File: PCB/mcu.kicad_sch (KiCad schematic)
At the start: 15 parts

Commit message: ok stm32
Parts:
- removed C? (x5): 100n, symbol Device:C
- removed C?: 10n, symbol Device:C
- removed C? (x3): 1u, symbol Device:C
- removed C?: 2.7u, symbol Device:C
- removed C?: 10u, symbol Device:C
- removed FB?: FerriteBead, symbol Device:FerriteBead
- removed R?: 1, symbol Device:R
- removed U?: EFM32PG22C200F128IM32-C, Package_DFN_QFN:QFN-32-1EP_4x4mm_P0.4mm_EP2.9x2.9mm, symbol TattooSupplyLib:EFM32PG22C200F128IM32-C
- added C? (x5): 100n, symbol Device:C
- added C? (x2): 20p, symbol Device:C
- added C?: 1u, symbol Device:C
- added C?: 10n, symbol Device:C
- added C?: 4.7u, symbol Device:C
- added FB?: FerriteBead, symbol Device:FerriteBead
- added J?: Conn_ARM_SWD_TagConnect_TC2030-NL, Connector:Tag-Connect_TC2030-IDC-NL_2x03_P1.27mm_Vertical, symbol Connector:Conn_ARM_SWD_TagConnect_TC2030-NL
- added JP?: Jumper_3_Open, symbol Jumper:Jumper_3_Open
- added NT?: NetTie_2, symbol Device:NetTie_2
- added R?: 10k, symbol Device:R
- added R? (x3): 100k, symbol Device:R
- added R?: R, symbol Device:R
- added R?: DNP, symbol Device:R
- added R? (x2): 4.7k, symbol Device:R
- added SW?: SW_Push, symbol Switch:SW_Push
- added U?: STM32F103C8Tx, Package_QFP:LQFP-48_7x7mm_P0.5mm, symbol MCU_ST_STM32F1:STM32F103C8Tx
- added Y?: Crystal, symbol Device:Crystal
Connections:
- net GND: now also J?.3 (GND), J?.5 (GND), J?.9 (GNDDetect), C?.2, C?.2, C?.2, C?.2, C?.2, C?.2, C?.2, C?.2, C?.2, C?.2, J?.5 (GND), JP?.3 (B), NT?.1, R?.1, R?.2, SW?.2, U?.23 (VSS), U?.35 (VSS), U?.47 (VSS)
- net V_{IN}: now reaches J?.1 (VTref)
- net V_{IN}: now also C?.1, C?.1, C?.1, C?.1, C?.1, FB?.1, J?.1 (VCC), JP?.1 (A), R?.1, R?.1, R?.1, R?.1, U?.1 (VBAT), U?.24 (VDD), U?.36 (VDD), U?.48 (VDD)
- net ~{RESET}: now reaches J?.10 (~{RESET})
- net ~{RESET}: now also C?.1, J?.3 (~{RESET}), R?.2, SW?.1, U?.7 (NRST)
- net SWDIO: now reaches J?.2 (SWDIO/TMS)
- net SWDIO: now also J?.2 (SWDIO), U?.34 (PA13)
- net SWCLK: now reaches J?.4 (SWDCLK/TCK)
- net SWCLK: now also J?.4 (SWCLK), U?.37 (PA14)
- new net: C?.1, R?.1, Y?.2
- new net: R?.2, U?.20 (PB2)
- new net: JP?.2 (C), R?.2
- new net: R?.1, R?.2, U?.44 (BOOT0)
- new net: NT?.2, U?.8 (VSSA)
- new net Analog1: U?.10 (PA0)
- new net Analog2: U?.11 (PA1)
- new net Display.MISO: U?.16 (PA6)
- new net Display.MOSI: U?.17 (PA7)
- new net Display.SCK: U?.15 (PA5)
- new net Display.~{CS}: U?.14 (PA4)
- new net I2C.SCL: R?.2, U?.42 (PB6)
- new net I2C.SDA: R?.2, U?.43 (PB7)
- new net OSC_{IN}: C?.1, U?.5 (PD0), Y?.1
- new net OSC_{OUT}: R?.2, U?.6 (PD1)
- new net SW1: U?.29 (PA8)
- new net SW2: U?.30 (PA9)
- new net USB.D+: U?.33 (PA12)
- new net USB.D-: U?.32 (PA11)
- new net USB_DFU: R?.1, U?.38 (PA15)
- new net VDDA: C?.1, C?.1, FB?.2, U?.9 (VDDA)
- no-connect marks 1 -> 22
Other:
- note added: "AN2867 : ECS-80-18-5PX-TR NX5032GA-8.000M-STD-CSU-1 BEST"
- note removed: "AVDD"
- note removed: "DVDD"
- note removed: "EFM32PG22C200F128IM32-C"
- note removed: "IOVDD"
- note removed: "VREG_{VDD}"
- moved on the sheet: J?

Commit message: continue quartz
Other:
- note added: "AN2867 : ABM3B-8.000MHZ-B2-T C_{L}=18pF C_{S}=10pF C_{L}-C_{S}=(C_{L1}*"
- note removed: "AN2867 : ECS-80-18-5PX-TR NX5032GA-8.000M-STD-CSU-1 BEST"
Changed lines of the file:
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@@
     (stroke (width 0) (type default) (color 0 0 0 0))
   )
-  (text "AN2867 :\nECS-80-18-5PX-TR\nNX5032GA-8.000M-STD-CSU-1 BEST\n"
+  (text "AN2867 :\nABM3B-8.000MHZ-B2-T\nC_{L}=18pF\nC_{S}=10pF\nC_{L}-C_{S}=(C_{L1}*\n"
     (at 21.59 101.6 0)
     (effects (font (size 1.27 1.27)) (justify left bottom))

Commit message: ok mcu
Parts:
- removed J?: Conn_ARM_JTAG_SWD_10, symbol Connector:Conn_ARM_JTAG_SWD_10
- removed R?: 10k, symbol Device:R
- added C? (x3): 100n, symbol Device:C
- added J?: Conn_ST_STDC14, symbol Connector:Conn_ST_STDC14
- added J?: Conn_01x03, symbol Connector_Generic:Conn_01x03
- added R? (x3): 10k, symbol Device:R
- added R? (x2): 20, symbol Device:R
- added SW?: RotaryEncoder_Switch, symbol Device:RotaryEncoder_Switch
- R?: value R -> 953
- Y?: value Crystal -> ABM3B-8.000MHZ-B2-T; footprint (none) -> Crystal:Crystal_SMD_Abracon_ABM3B-4Pin_5.0x3.2mm
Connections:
- net GND: now also C?.1, C?.2, C?.2, J?.11 (GNDDetect), J?.3 (Pin_3), J?.5 (GND), J?.7 (GND), SW?.C, SW?.S2
- net SW1: now also R?.2; no longer U?.29 (PA8)
- net SW2: now also R?.2; no longer U?.30 (PA9)
- net SWCLK: now also J?.6 (JCLK/SWCLK)
- net SWDIO: now also J?.4 (JTMS/SWDIO)
- net V_{IN}: now also J?.3 (VCC), R?.1, R?.2, R?.2
- net ~{RESET}: now also J?.12 (~{RST})
- net Debug.Tx: now reaches U?.12 (PA2)
- net Debug.Tx: now also J?.1 (Pin_1), J?.14 (VCP_TX)
- net Debug.Rx: now reaches U?.13 (PA3)
- net Debug.Rx: now also J?.13 (VCP_RX), J?.2 (Pin_2)
- net Encod.DT: now reaches U?.26 (PB13)
- net Encod.DT: now also C?.2, R?.1, SW?.A
- net Encod.CLK: now reaches U?.27 (PB14)
- net Encod.CLK: now also C?.1, R?.2, SW?.B
- net Encod.SW: now reaches U?.28 (PB15)
- net Encod.SW: now also C?.1, R?.1, SW?.S1
- new net: R?.1, U?.29 (PA8)
- new net: R?.1, U?.30 (PA9)
- no-connect marks 22 -> 18
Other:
- note added: "AN2867 : ABM3B-8.000MHZ-B2-T C_{L}=18pF C_{S}=7-10pF C_{L}-C_{S}=C_{L1}*C_{L2}/(C_{L1}+C_{L2})=10pF C_{L1}=C_{L2}=20pF R_{EXT}=1/(2*pi*F*C_{L2})=994ohm"
- note removed: "AN2867 : ABM3B-8.000MHZ-B2-T C_{L}=18pF C_{S}=10pF C_{L}-C_{S}=(C_{L1}*"

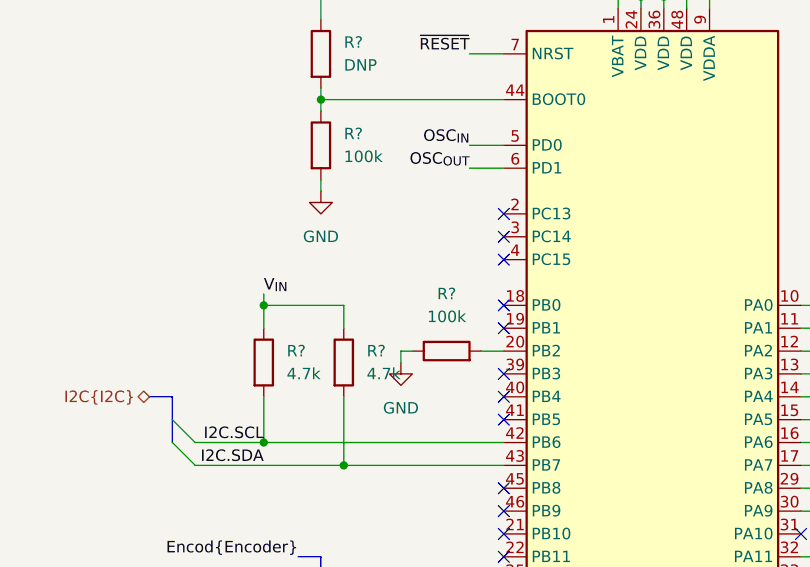
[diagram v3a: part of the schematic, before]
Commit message: add mcu on off smps
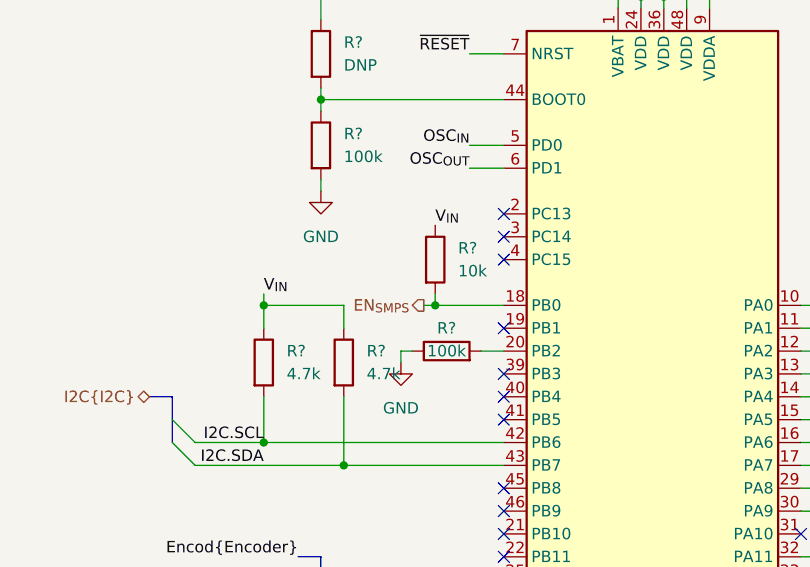
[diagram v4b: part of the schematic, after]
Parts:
- added R?: 10k, symbol Device:R
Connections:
- net V_{IN}: now also R?.1
- net EN_{SMPS}: now reaches U?.18 (PB0)
- net EN_{SMPS}: now also R?.2
- no-connect marks 18 -> 17
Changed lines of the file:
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@@
   (junction (at 104.14 110.49) (diameter 0) (color 0 0 0 0)
+  )
+  (junction (at 123.19 95.25) (diameter 0) (color 0 0 0 0)
   )
   (junction (at 104.14 95.25) (diameter 0) (color 0 0 0 0)
@@
   (no_connect (at 130.81 97.79))
   (no_connect (at 130.81 90.17))
-  (no_connect (at 130.81 95.25))
   (no_connect (at 130.81 87.63))
   (no_connect (at 130.81 85.09))
@@
     (stroke (width 0) (type default) (color 0 0 0 0))
   )
+  (wire (pts (xy 121.92 95.25) (xy 123.19 95.25))
+    (stroke (width 0) (type default) (color 0 0 0 0))
+  )
   (wire (pts (xy 96.52 110.49) (xy 104.14 110.49))
     (stroke (width 0) (type default) (color 0 0 0 0))
@@
     (stroke (width 0) (type default) (color 0 0 0 0))
   )
+  (wire (pts (xy 123.19 95.25) (xy 130.81 95.25))
+    (stroke (width 0) (type default) (color 0 0 0 0))
+  )
   (wire (pts (xy 96.52 113.03) (xy 113.03 113.03))
     (stroke (width 0) (type default) (color 0 0 0 0))
@@
   )
   (wire (pts (xy 214.63 146.05) (xy 215.9 146.05))
+    (stroke (width 0) (type default) (color 0 0 0 0))
+  )
+  (wire (pts (xy 123.19 93.98) (xy 123.19 95.25))
     (stroke (width 0) (type default) (color 0 0 0 0))
   )
@@
     (effects (font (size 1.27 1.27)) (justify right bottom))
   )
+  (label "V_{IN}" (at 123.19 86.36 0)
+    (effects (font (size 1.27 1.27)) (justify left bottom))
+  )
   (label "~{RESET}" (at 228.6 63.5 180)
     (effects (font (size 1.27 1.27)) (justify right bottom))
@@
   (hierarchical_label "USB{USB2}" (shape bidirectional) (at 185.42 120.65 0)
     (effects (font (size 1.27 1.27)) (justify left))
+  )
+  (hierarchical_label "EN_{SMPS}" (shape output) (at 121.92 95.25 180)
+    (effects (font (size 1.27 1.27)) (justify right))
   )
   (hierarchical_label "V_{IN}" (shape input) (at 36.83 20.32 180)
@@
   )
   (symbol (lib_id "Device:R") (at 124.46 100.33 90) (unit 1)
-    (in_bom yes) (on_board yes) (fields_autoplaced)
-    (property "Reference" "R?" (id 0) (at 124.46 93.98 90))
-    (property "Value" "100k" (id 1) (at 124.46 96.52 90))
+    (in_bom yes) (on_board yes)
+    (property "Reference" "R?" (id 0) (at 124.46 97.79 90))
+    (property "Value" "100k" (id 1) (at 124.46 100.33 90))
     (property "Footprint" "" (id 2) (at 124.46 102.108 90)
       (effects (font (size 1.27 1.27)) hide)
@@
     (pin "1")
   )
+  (symbol (lib_id "Device:R") (at 123.19 90.17 0) (unit 1)
+    (in_bom yes) (on_board yes) (fields_autoplaced)
+    (property "Reference" "R?" (id 0) (at 125.73 88.8999 0)
+      (effects (font (size 1.27 1.27)) (justify left))
+    )
+    (property "Value" "10k" (id 1) (at 125.73 91.4399 0)
+      (effects (font (size 1.27 1.27)) (justify left))
+    )
+    (property "Footprint" "" (id 2) (at 121.412 90.17 90)
+      (effects (font (size 1.27 1.27)) hide)
+    )
+    (property "Datasheet" "~" (id 3) (at 123.19 90.17 0)
+      (effects (font (size 1.27 1.27)) hide)
+    )
+    (pin "1")
+    (pin "2")
+  )
   (symbol (lib_id "MCU_ST_STM32F1:STM32F103C8Tx") (at 148.59 100.33 0) (unit 1)
